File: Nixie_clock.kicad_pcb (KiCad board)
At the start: 2 copper layers, 29 parts, among them J1 Screw_Terminal_01x02, J2 Screw_Terminal_01x03, U1 74HCT04, U10 TPIC6B595, U11 TPIC6B595, U2 TPIC6B595, U3 Pollin_DCF1, U4 TPIC6B595, U5 WeMos_D1_mini, U6 TPIC6B595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

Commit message: First version of complete board
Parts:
- added H1: MountingHole, MountingHole:MountingHole_4.3mm_M4, F.Cu at (75.6, 73.8)
- added H2: MountingHole, MountingHole:MountingHole_4.3mm_M4, F.Cu at (216.7, 73.8)
- added H3: MountingHole, MountingHole:MountingHole_4.3mm_M4, F.Cu at (195.2, 95.4)
- added H4: MountingHole, MountingHole:MountingHole_4.3mm_M4, F.Cu at (147.2, 123.5)
- C1, R4, U1: moved to B.Cu
- U3: footprint Connector_PinSocket_2.54mm:PinSocket_1x04_P2.54mm_Horizontal -> Connector_PinSocket_2.54mm:PinSocket_1x04_P2.54mm_Vertical; moved to B.Cu
- moved U2 185.5 mm to (229.4, 64.5), turned to 180 degrees
- moved N1 183.6 mm to (228.1, 82.7), turned to 0 degrees
- moved R1 165.8 mm to (217.1, 88.5), turned to 90 degrees
- moved U4 138.7 mm to (205.8, 64.5), turned to 180 degrees
- moved R3 134.8 mm to (212.3, 88.5), turned to 90 degrees
- moved N2 133.8 mm to (202.1, 82.7), turned to 0 degrees
- moved U11 132.5 mm to (64.0, 64.5), turned to 180 degrees
- moved N6 124.2 mm to (64.1, 82.7), turned to 0 degrees
- moved J1 120.9 mm to (197.1, 109.5), turned to 90 degrees
- moved J2 119.7 mm to (197.1, 127.0), turned to 90 degrees
- moved U1 104.2 mm to (185.3, 93.0), turned to -90 degrees
- moved R8 103.3 mm to (74.9, 89.2), turned to 90 degrees
- moved U6 92.1 mm to (182.2, 64.5), turned to 180 degrees
- moved U10 87.2 mm to (87.6, 64.5), turned to 180 degrees
- moved R5 67.0 mm to (172.5, 88.1), turned to 90 degrees
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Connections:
- net Net-(N1-PadA) renamed /N1-A
- net Net-(N2-PadA) renamed /N2-A
- net Net-(N3-PadA) renamed /N3-A
- net Net-(N4-PadA) renamed /N4-A
- net Net-(N5-PadA) renamed /N5-A
- net Net-(N6-PadA) renamed /N6-A
- net Net-(U10-DRAIN0) renamed /U10-D0
- net Net-(U10-DRAIN1) renamed /U10-D1
- net Net-(U10-DRAIN2) renamed /U10-D2
- net Net-(U10-DRAIN3) renamed /U10-D3
- net Net-(U10-DRAIN4) renamed /U10-D4
- net Net-(U10-DRAIN5) renamed /U10-D5
- net Net-(U10-DRAIN6) renamed /U10-D6
- net Net-(U10-DRAIN7) renamed /U10-D7
- net Net-(U11-DRAIN0) renamed /U11-D0
- net Net-(U11-DRAIN1) renamed /U11-D1
- net Net-(U11-DRAIN2) renamed /U11-D2
- net Net-(U11-DRAIN3) renamed /U11-D3
- net Net-(U2-DRAIN0) renamed /U2-D0
- net Net-(U2-DRAIN1) renamed /U2-D1
- net Net-(U2-DRAIN2) renamed /U2-D2
- net Net-(U2-DRAIN3) renamed /U2-D3
- net Net-(U2-DRAIN4) renamed /U2-D4
- net Net-(U2-DRAIN5) renamed /U2-D5
- net Net-(U2-DRAIN6) renamed /U2-D6
- net Net-(U2-DRAIN7) renamed /U2-D7
- net Net-(U4-DRAIN0) renamed /U4-D0
- net Net-(U4-DRAIN1) renamed /U4-D1
- net Net-(U4-DRAIN2) renamed /U4-D2
- net Net-(U4-DRAIN3) renamed /U4-D3
- net Net-(U4-DRAIN4) renamed /U4-D4
- net Net-(U4-DRAIN5) renamed /U4-D5
- net Net-(U4-DRAIN6) renamed /U4-D6
- net Net-(U4-DRAIN7) renamed /U4-D7
- net Net-(U6-DRAIN0) renamed /U6-D0
- net Net-(U6-DRAIN1) renamed /U6-D1
- net Net-(U6-DRAIN2) renamed /U6-D2
- net Net-(U6-DRAIN3) renamed /U6-D3
- net Net-(U6-DRAIN4) renamed /U6-D4
- net Net-(U6-DRAIN5) renamed /U6-D5
- net Net-(U6-DRAIN6) renamed /U6-D6
- net Net-(U6-DRAIN7) renamed /U6-D7
- net Net-(U7-DRAIN0) renamed /U7-D0
- net Net-(U7-DRAIN1) renamed /U7-D1
- net Net-(U7-DRAIN2) renamed /U7-D2
- net Net-(U7-DRAIN3) renamed /U7-D3
- net Net-(U7-DRAIN4) renamed /U7-D4
- net Net-(U7-DRAIN5) renamed /U7-D5
- net Net-(U7-DRAIN6) renamed /U7-D6
- net Net-(U7-DRAIN7) renamed /U7-D7
- net Net-(U8-DRAIN0) renamed /U8-D0
- net Net-(U8-DRAIN1) renamed /U8-D1
- net Net-(U8-DRAIN2) renamed /U8-D2
- net Net-(U8-DRAIN3) renamed /U8-D3
- net Net-(U8-DRAIN4) renamed /U8-D4
- net Net-(U8-DRAIN5) renamed /U8-D5
- net Net-(U8-DRAIN6) renamed /U8-D6
- net Net-(U8-DRAIN7) renamed /U8-D7
- net Net-(U9-DRAIN0) renamed /U9-D0
- net Net-(U9-DRAIN1) renamed /U9-D1
- net Net-(U9-DRAIN2) renamed /U9-D2
- net Net-(U9-DRAIN3) renamed /U9-D3
- net Net-(U9-DRAIN4) renamed /U9-D4
- net Net-(U9-DRAIN5) renamed /U9-D5
- net Net-(U9-DRAIN6) renamed /U9-D6
- net Net-(U9-DRAIN7) renamed /U9-D7
- U1 pad 1: Net-(U5-CS/D8) -> Net-(U1-Pad1)
- U1 pad 10: Net-(U10-RCLK) -> Net-(U1-Pad10)
- U1 pad 11: Net-(U1-Pad11) -> Net-(U5-MOSI/D7)
- U1 pad 12: Net-(U2-SER_IN) -> Net-(U1-Pad1)
- U1 pad 13: Net-(U1-Pad13) -> Net-(U5-SCK/D5)
- U1 pad 2: Net-(U1-Pad11) -> Net-(U10-SRCK)
- U1 pad 3: Net-(U5-MOSI/D7) -> Net-(U1-Pad3)
- U1 pad 4: Net-(U1-Pad13) -> Net-(U10-RCLK)
- U1 pad 5: Net-(U5-SCK/D5) -> Net-(U1-Pad10)
- U1 pad 6: Net-(U1-Pad6) -> Net-(U2-SER_IN)
- U1 pad 8: Net-(U10-SRCK) -> Net-(U1-Pad3)
- U1 pad 9: Net-(U1-Pad6) -> Net-(U5-CS/D8)
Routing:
- net +5V: track 0.00 -> 375.3 mm, vias 0 -> 18
- net Net-(U10-RCLK): track 0.00 -> 211.2 mm, vias 0 -> 8
- net Net-(U10-SRCK): track 0.00 -> 209.5 mm, vias 0 -> 9
- net 167V: track 0.00 -> 174.3 mm
- net Net-(U2-SER_IN): track 0.00 -> 71.2 mm, vias 0 -> 1
- net /U10-D4: track 0.00 -> 38.8 mm
- net /U10-D5: track 0.00 -> 38.6 mm
- net /U10-D3: track 0.00 -> 38.5 mm
- net /U10-D6: track 0.00 -> 37.3 mm
- net /U10-D2: track 0.00 -> 37.1 mm
- net /U9-D3: track 0.00 -> 36.5 mm
- net /U9-D0: track 0.00 -> 35.8 mm
- net /U7-D6: track 0.00 -> 35.4 mm
- net /U6-D3: track 0.00 -> 35.0 mm
- net /U4-D1: track 0.00 -> 34.7 mm
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- added copper zone on B.Cu, net GND
- added copper zone on F.Cu, net GND
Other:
- board outline added: 185 x 73 mm
- board text removed: "Minimum Drill: 16mil (0.4mm) Minimum Trace: 15mil (0.38mm) High Voltage Clearance: 33mil (0.8mm)"

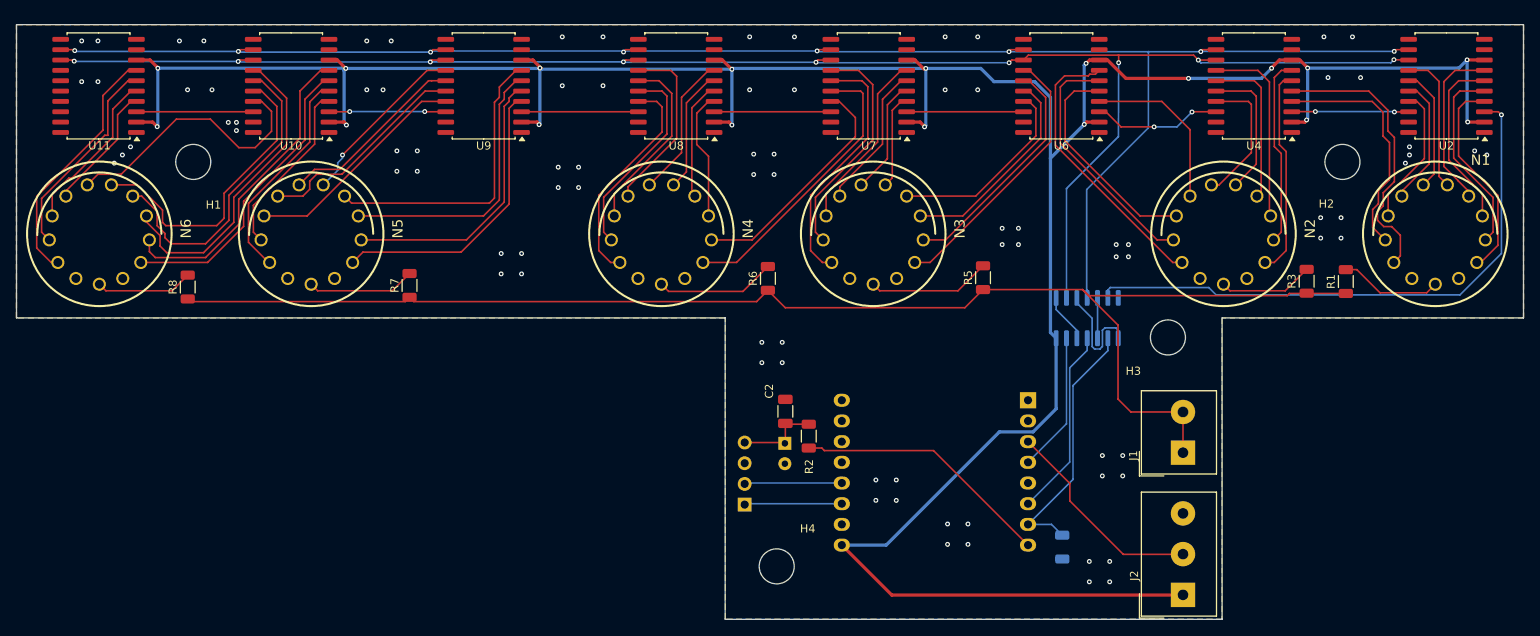
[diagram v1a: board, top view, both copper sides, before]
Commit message: The Nixie PSU now fits seemlessly into the bottom right corner of the PCB
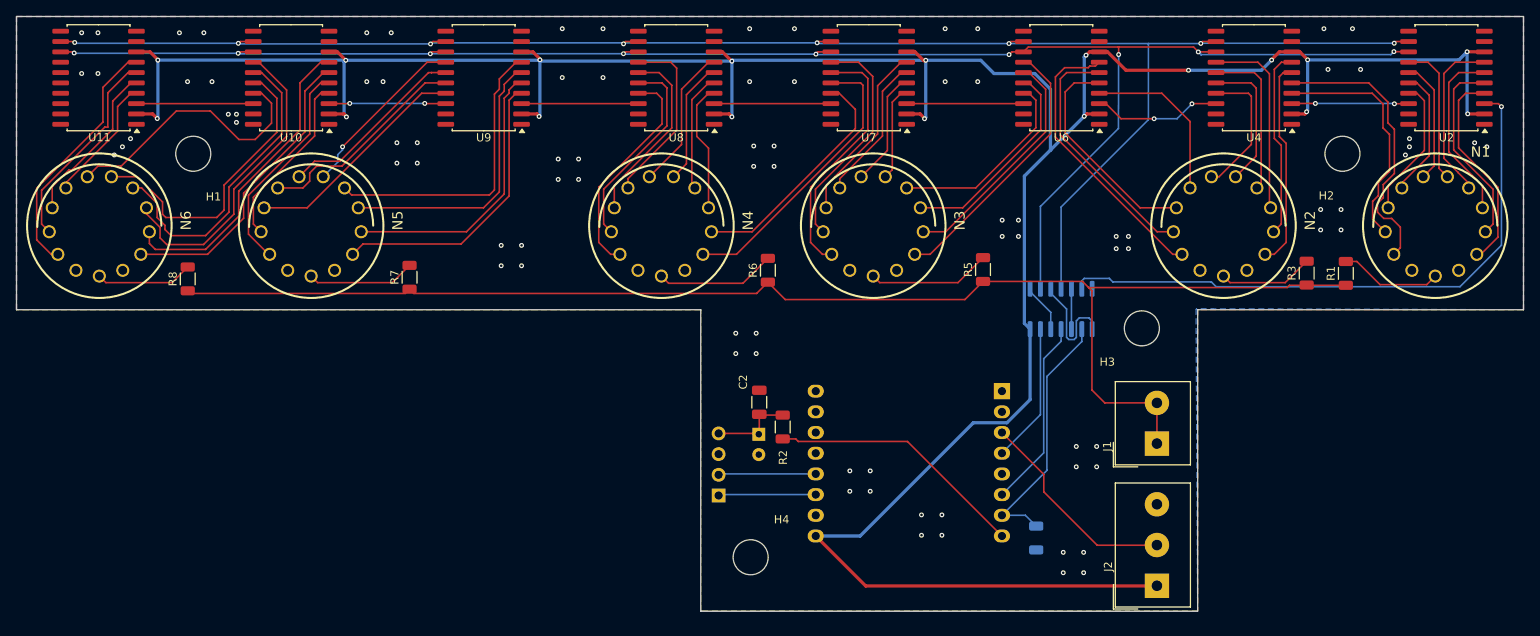
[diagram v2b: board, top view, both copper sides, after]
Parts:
- moved H4 3.39 mm to (144.0, 122.4)
- moved J1 3.39 mm to (193.9, 108.4)
- moved J2 3.39 mm to (193.9, 125.9)
- moved C1 3.39 mm to (145.0, 107.3)
- moved C2 3.39 mm to (145.1, 103.4)
- moved H3 3.39 mm to (192.0, 94.3)
- moved R2 3.39 mm to (147.9, 106.4)
- moved U1 3.39 mm to (182.1, 91.9)
- moved U3 3.39 mm to (140.1, 114.8)
- moved U5 3.39 mm to (174.9, 102.0)
- moved R4 3.39 mm to (179.1, 120.0)
- moved H1 1.00 mm to (75.6, 72.8)
- moved H2 1.00 mm to (216.7, 72.8)
- moved N1 1.00 mm to (228.1, 81.7)
- moved N2 1.00 mm to (202.1, 81.7)
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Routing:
- net Net-(U2-SER_IN): track 71.2 -> 74.4 mm
- net 167V: track 174.3 -> 171.8 mm
- net +5V: track 375.3 -> 376.7 mm
- net Net-(U10-SRCK): track 209.5 -> 210.7 mm
- net Net-(U10-RCLK): track 211.2 -> 212.4 mm
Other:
- outline, holes or cut-outs redrawn
